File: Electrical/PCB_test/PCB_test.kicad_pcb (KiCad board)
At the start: 2 copper layers, 43 parts, among them J1 Screw_Terminal_01x02

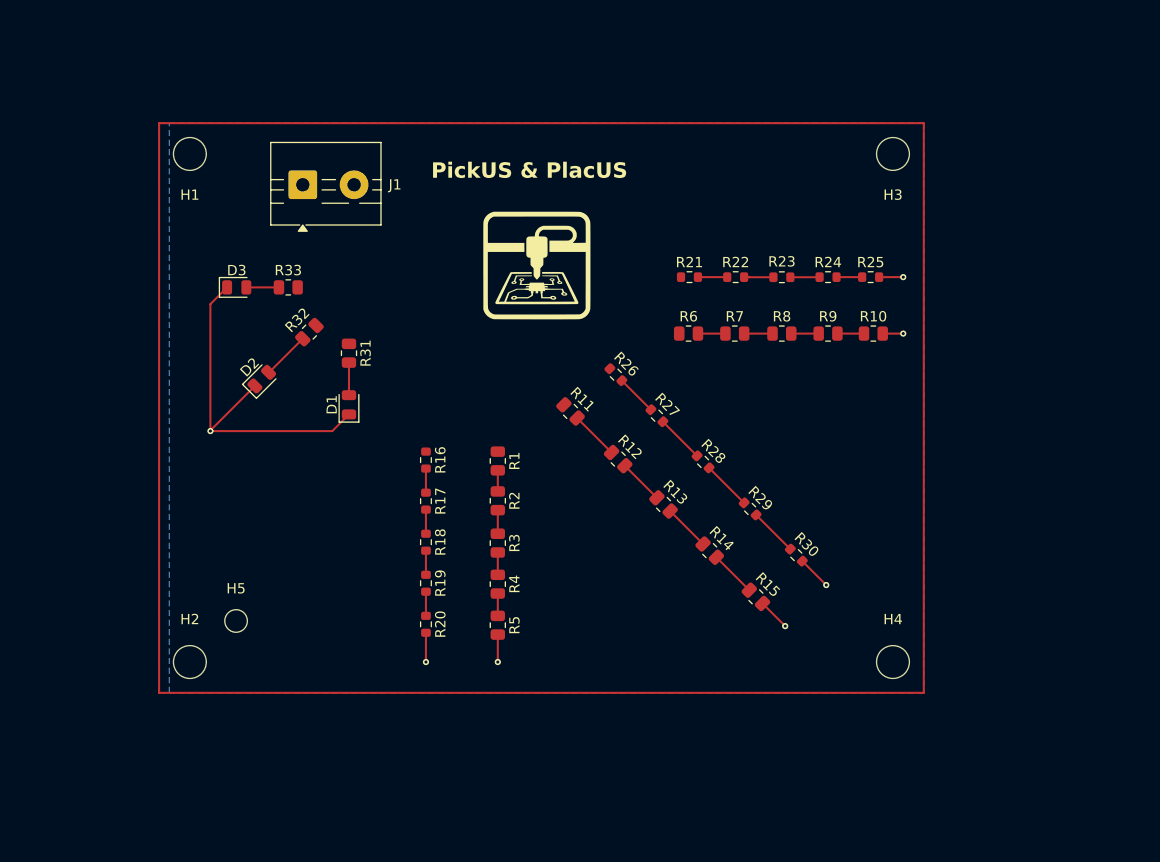
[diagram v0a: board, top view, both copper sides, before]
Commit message: edge cut is clean
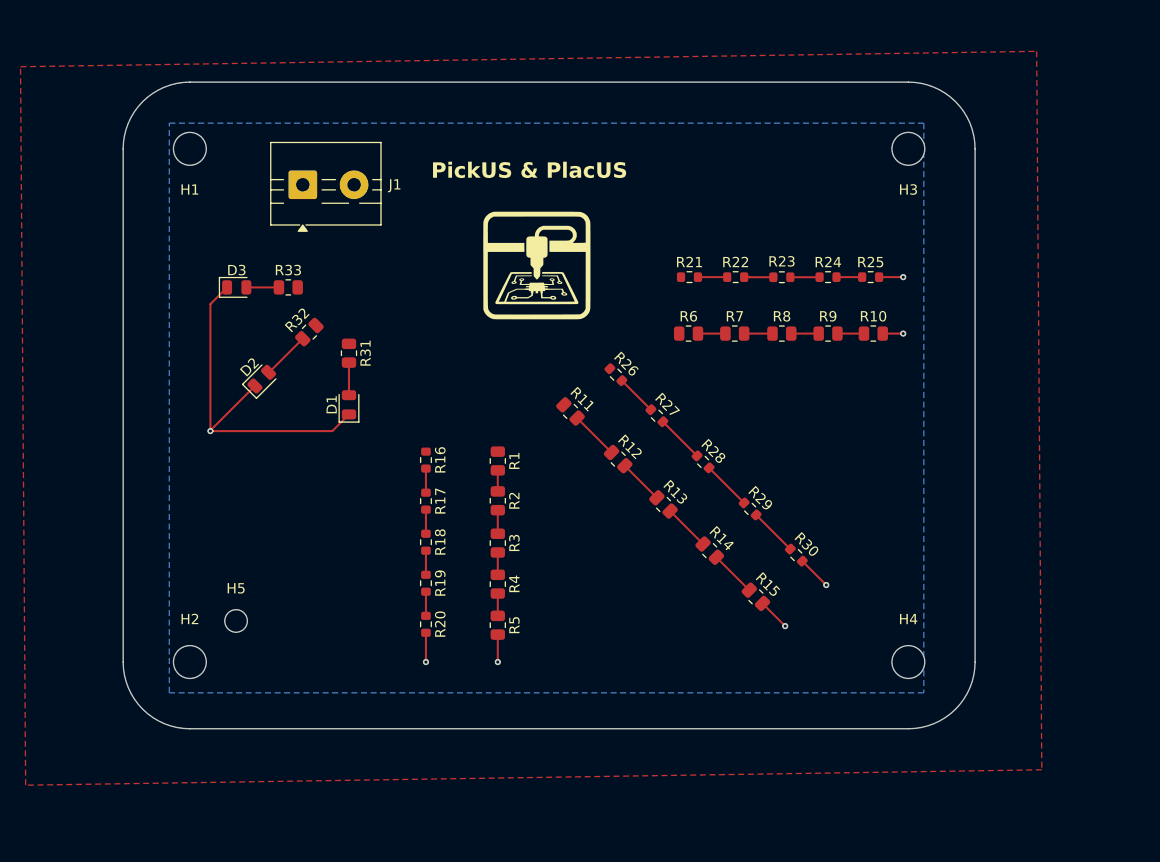
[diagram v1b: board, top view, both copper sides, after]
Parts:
- moved H3 1.58 mm to (116.5, 33.0)
- moved H4 1.50 mm to (116.5, 83.0)
- moved H1 0.50 mm to (46.5, 33.0)
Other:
- board outline added: 83 x 63 mm
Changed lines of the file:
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@@
 	(footprint "MountingHole:MountingHole_3.2mm_M3"
 		(layer "F.Cu")
-		(at 46.5 33.5)
+		(at 46.5 33)
 		(descr "Mounting Hole 3.2mm, M3, no annular, generated by kicad-footprint-generator mountinghole.py")
 		(tags "mountinghole M3")
@@
 	(footprint "MountingHole:MountingHole_3.2mm_M3"
 		(layer "F.Cu")
-		(at 115 33.5)
+		(at 116.5 33)
 		(descr "Mounting Hole 3.2mm, M3, no annular, generated by kicad-footprint-generator mountinghole.py")
 		(tags "mountinghole M3")
@@
 	(footprint "MountingHole:MountingHole_3.2mm_M3"
 		(layer "F.Cu")
-		(at 115 83)
+		(at 116.5 83)
 		(descr "Mounting Hole 3.2mm, M3, no annular, generated by kicad-footprint-generator mountinghole.py")
 		(tags "mountinghole M3")
@@
 		)
 	)
-	(gr_rect
-		(start 43.5 30.5)
-		(end 118 86)
+	(gr_line
+		(start 123 83)
+		(end 123 33)
 		(stroke
-			(width 0.2)
+			(width 0.05)
 			(type default)
 		)
-		(fill no)
-		(layer "F.Cu")
+		(layer "Edge.Cuts")
+	)
+	(gr_line
+		(start 116.5 26.5)
+		(end 46.5 26.5)
+		(stroke
+			(width 0.05)
+			(type default)
+		)
+		(layer "Edge.Cuts")
+	)
+	(gr_line
+		(start 46.5 89.5)
+		(end 116.5 89.5)
+		(stroke
+			(width 0.05)
+			(type default)
+		)
+		(layer "Edge.Cuts")
+	)
+	(gr_line
+		(start 40 33)
+		(end 40 83)
+		(stroke
+			(width 0.05)
+			(type default)
+		)
+		(layer "Edge.Cuts")
+	)
+	(gr_arc
+		(start 46.5 89.5)
+		(mid 41.903806 87.596194)
+		(end 40 83)
+		(stroke
+			(width 0.05)
+			(type default)
+		)
+		(layer "Edge.Cuts")
+	)
+	(gr_arc
+		(start 40 33)
+		(mid 41.903806 28.403806)
+		(end 46.5 26.5)
+		(stroke
+			(width 0.05)
+			(type default)
+		)
+		(layer "Edge.Cuts")
+	)
+	(gr_arc
+		(start 116.5 26.5)
+		(mid 121.096194 28.403806)
+		(end 123 33)
+		(stroke
+			(width 0.05)
+			(type default)
+		)
+		(layer "Edge.Cuts")
+	)
+	(gr_arc
+		(start 123 83)
+		(mid 121.096194 87.596194)
+		(end 116.5 89.5)
+		(stroke
+			(width 0.05)
+			(type default)
+		)
+		(layer "Edge.Cuts")
 	)
 	(gr_text "PickUS & PlacUS"
@@
 		)
 	)
+	(dimension
+		(type orthogonal)
+		(layer "Dwgs.User")
+		(pts
+			(xy 116.5 83) (xy 116.5 33)
+		)
+		(height 7.5)
+		(orientation 1)
+		(format
+			(prefix "")
+			(suffix "")
+			(units 3)
+			(units_format 0)
+			(precision 4)
+			(suppress_zeroes yes)
+		)
+		(style
+			(thickness 0.1)
+			(arrow_length 1.27)
+			(text_position_mode 0)
+			(arrow_direction outward)
+			(extension_height 0.58642)
+			(extension_offset 0.5)
+			(keep_text_aligned yes)
+		)
+		(gr_text "50"
+			(at 122.9 58 90)
+			(layer "Dwgs.User")
+			(effects
+				(font
+					(size 1 1)
+					(thickness 0.1)
+				)
+			)
+		)
+	)
+	(dimension
+		(type orthogonal)
+		(layer "Cmts.User")
+		(pts
+			(xy 46.5 33) (xy 116.5 33)
+		)
+		(height -5)
+		(orientation 0)
+		(format
+			(prefix "")
+			(suffix "")
+			(units 3)
+			(units_format 0)
+			(precision 4)
+			(suppress_zeroes yes)
+		)
+		(style
+			(thickness 0.1)
+			(arrow_length 1.27)
+			(text_position_mode 0)
+			(arrow_direction outward)
+			(extension_height 0.58642)
+			(extension_offset 0.5)
+			(keep_text_aligned yes)
+		)
+		(gr_text "70"
+			(at 81.5 26.9 0)
+			(layer "Cmts.User")
+			(effects
+				(font
+					(size 1 1)
+					(thickness 0.1)
+				)
+			)
+		)
+	)
+	(dimension
+		(type orthogonal)
+		(layer "Cmts.User")
+		(pts
+			(xy 46.5 83) (xy 116.5 83)
+		)
+		(height 8)
+		(orientation 0)
+		(format
+			(prefix "")
+			(suffix "")
+			(units 3)
+			(units_format 0)
+			(precision 4)
+			(suppress_zeroes yes)
+		)
+		(style
+			(thickness 0.1)
+			(arrow_length 1.27)
+			(text_position_mode 0)
+			(arrow_direction outward)
+			(extension_height 0.58642)
+			(extension_offset 0.5)
+			(keep_text_aligned yes)
+		)
+		(gr_text "70"
+			(at 81.5 89.9 0)
+			(layer "Cmts.User")
+			(effects
+				(font
+					(size 1 1)
+					(thickness 0.1)
+				)
+			)
+		)
+	)
+	(dimension
+		(type orthogonal)
+		(layer "Cmts.User")
+		(pts
+			(xy 46.5 83) (xy 46.5 33)
+		)
+		(height -11)
+		(orientation 1)
+		(format
+			(prefix "")
+			(suffix "")
+			(units 3)
+			(units_format 0)
+			(precision 4)
+			(suppress_zeroes yes)
+		)
+		(style
+			(thickness 0.1)
+			(arrow_length 1.27)
+			(text_position_mode 0)
+			(arrow_direction outward)
+			(extension_height 0.58642)
+			(extension_offset 0.5)
+			(keep_text_aligned yes)
+		)
+		(gr_text "50"
+			(at 34.4 58 90)
+			(layer "Cmts.User")
+			(effects
+				(font
+					(size 1 1)
+					(thickness 0.1)
+				)
+			)
+		)
+	)
 	(segment
 		(start 62 58.875002)
@@
 		(polygon
 			(pts
-				(xy 43.5 30.5) (xy 118 30.5) (xy 118 86) (xy 43.5 86)
+				(xy 30 25) (xy 129 23.5) (xy 129.5 93.5) (xy 30.5 95)
 			)
 		)

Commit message: reference hole added
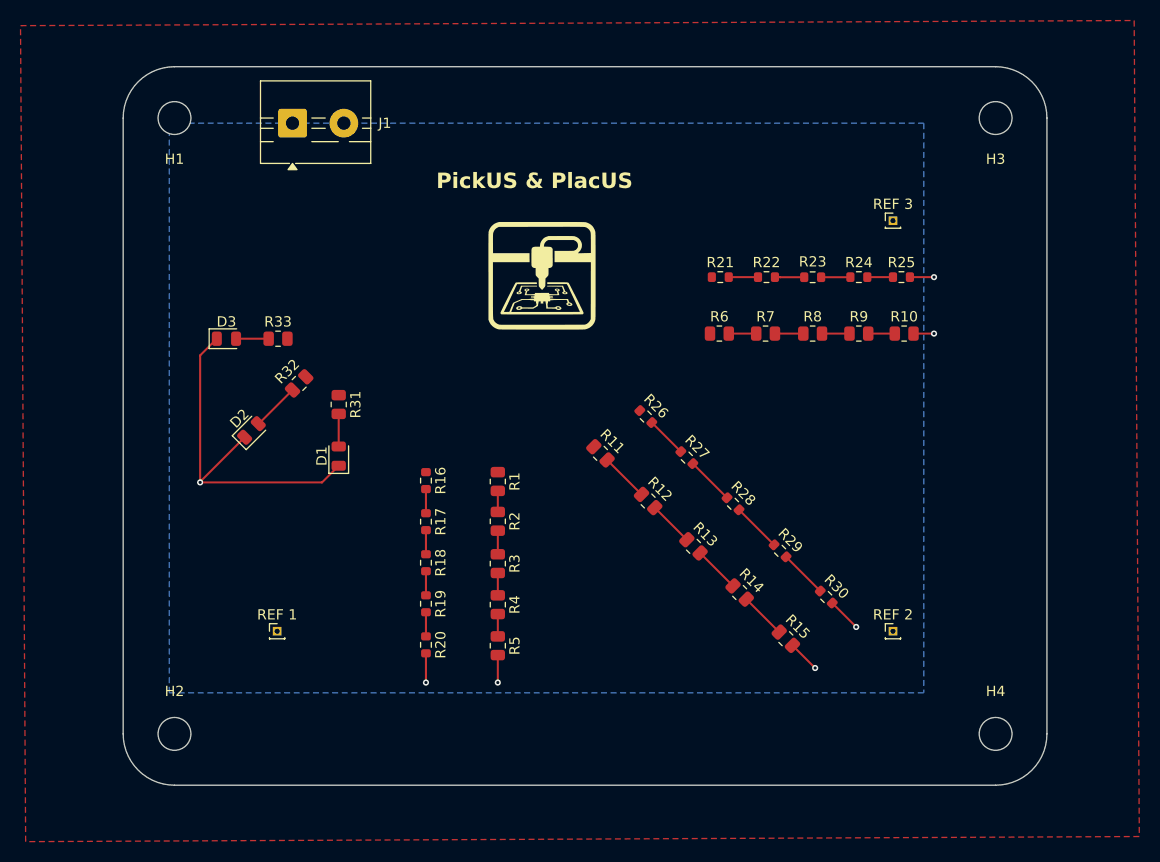
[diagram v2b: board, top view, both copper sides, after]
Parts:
- removed H5: MountingHole, MountingHole:MountingHole_2.2mm_M2
- added REF 1: Conn_01x01_Pin, Connector_PinHeader_1.00mm:PinHeader_1x01_P1.00mm_Vertical, F.Cu at (55.0, 80.0)
- added REF 2: Conn_01x01_Pin, Connector_PinHeader_1.00mm:PinHeader_1x01_P1.00mm_Vertical, F.Cu at (115.0, 80.0)
- added REF 3: Conn_01x01_Pin, Connector_PinHeader_1.00mm:PinHeader_1x01_P1.00mm_Vertical, F.Cu at (115.0, 40.0)
- moved H4 11.0 mm to (125.0, 90.0)
- moved H3 9.01 mm to (125.0, 30.0)
- moved H2 7.16 mm to (45.0, 90.0)
- moved J1 6.08 mm to (56.5, 30.5)
- moved D1 5.10 mm to (61.0, 62.9)
- moved D2 5.10 mm to (52.5, 60.4)
- moved D3 5.10 mm to (50.1, 51.5)
- moved R31 5.10 mm to (61.0, 57.9)
- moved R32 5.10 mm to (57.1, 55.9)
- moved R33 5.10 mm to (55.1, 51.5)
- moved R13 5.02 mm to (95.6, 71.7)
- moved R14 5.02 mm to (100.1, 76.2)
- moved R15 5.02 mm to (104.6, 80.7)
- moved R28 5.02 mm to (99.4, 67.6)
- moved R11 5.02 mm to (86.5, 62.7)
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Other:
- board size 83 x 63 mm -> 90 x 70 mm
